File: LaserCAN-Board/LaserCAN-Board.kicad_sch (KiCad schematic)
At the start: 34 parts, among them J2 TC2050-IDC-NL, U10 M24C64-RMN6TP, U2 VL53L1CXV0FY1, U4 STM32F103C8Tx, U5 MCP1703Ax-330xxTT, U9 SN65HVD230

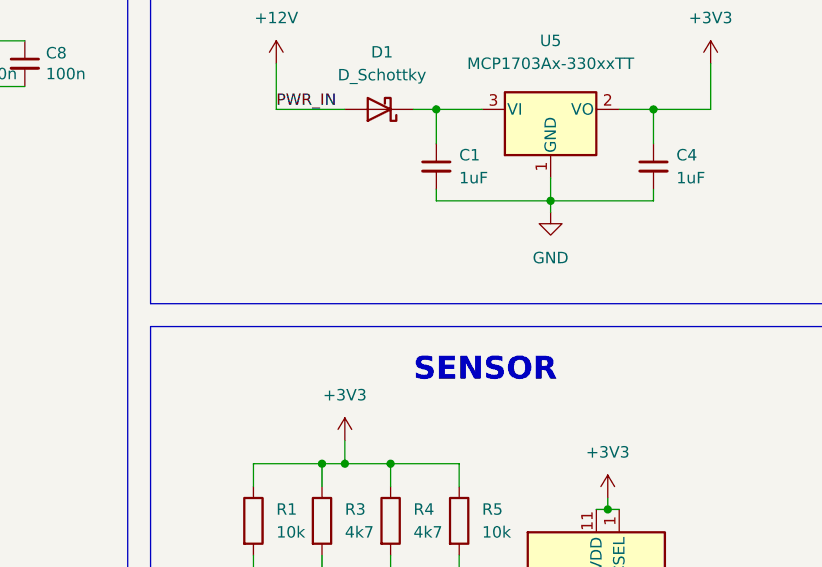
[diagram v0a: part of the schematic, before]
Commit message: Add PDF Schematic
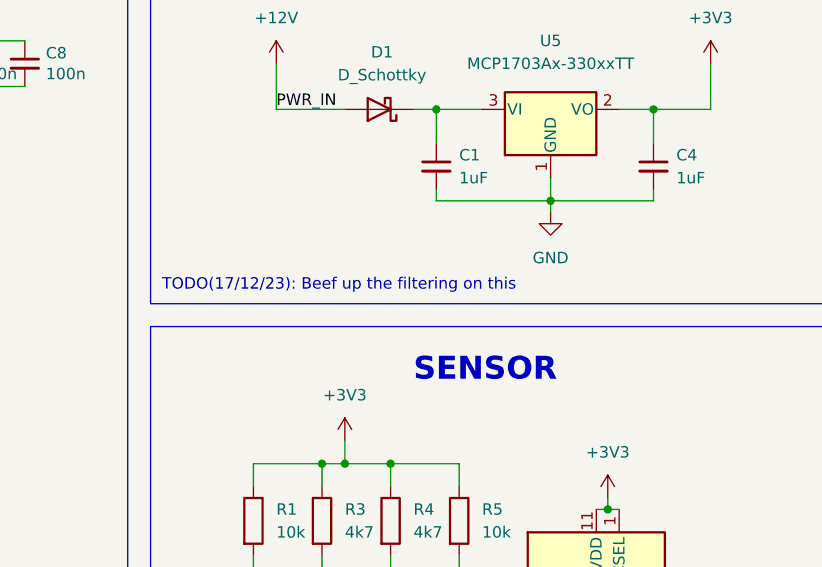
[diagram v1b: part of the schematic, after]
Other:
- note added: "TODO(17/12/23): Beef up the filtering on this"
- company: (none) -> Grapple Robotics
- title: (none) -> LaserCAN
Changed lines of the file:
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@@
 (kicad_sch (version 20230121) (generator eeschema)
   (paper "A4")
+  (title_block
+    (title "LaserCAN")
+    (rev "3")
+    (company "Grapple Robotics")
+    (comment 1 "https://grapplerobotics.au")
+    (comment 2 "https://github.com/GrappleRobotics/LaserCAN")
+  )
   (junction (at 203.2 111.76) (diameter 0) (color 0 0 0 0)
   )
@@
     (effects (font (size 2.54 2.54) (thickness 0.508) bold) (justify left bottom))
   )
+  (text "TODO(17/12/23): Beef up the filtering on this" (at 153.67 57.15 0)
+    (effects (font (size 1.27 1.27)) (justify left bottom))
+  )
   (label "CAN_RX" (at 106.68 69.85 180) (fields_autoplaced)

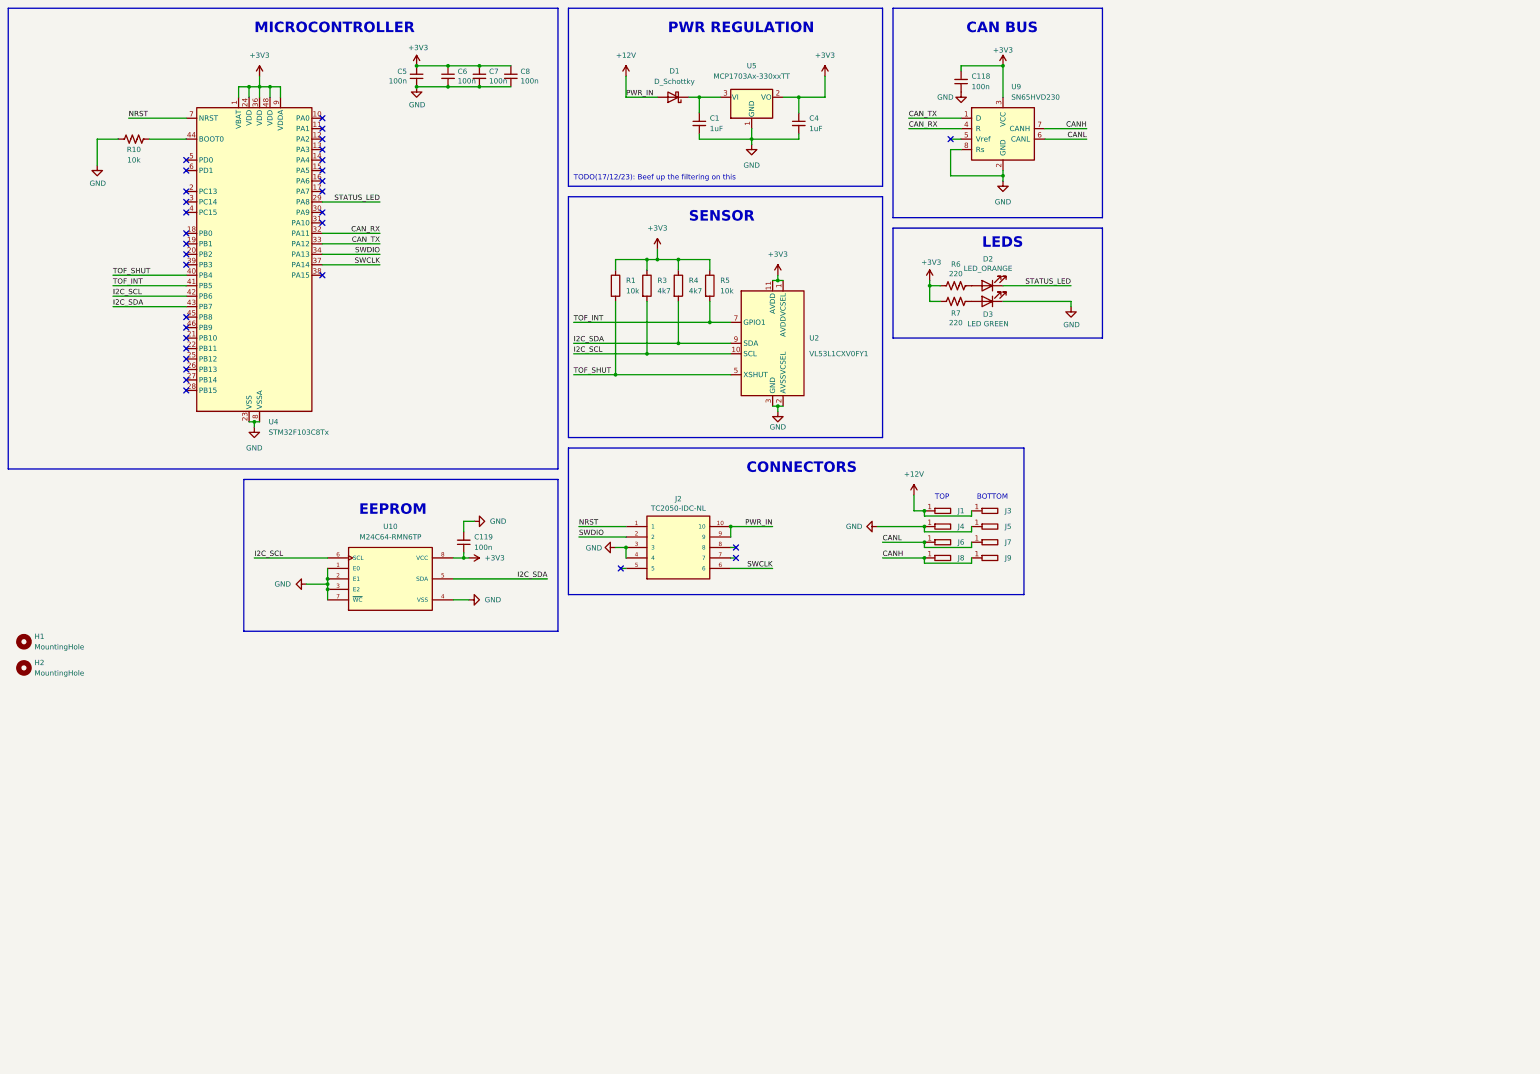
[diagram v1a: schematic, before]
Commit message: Update to v3.1 - Improved voltage regulation performance, improved ESD protection
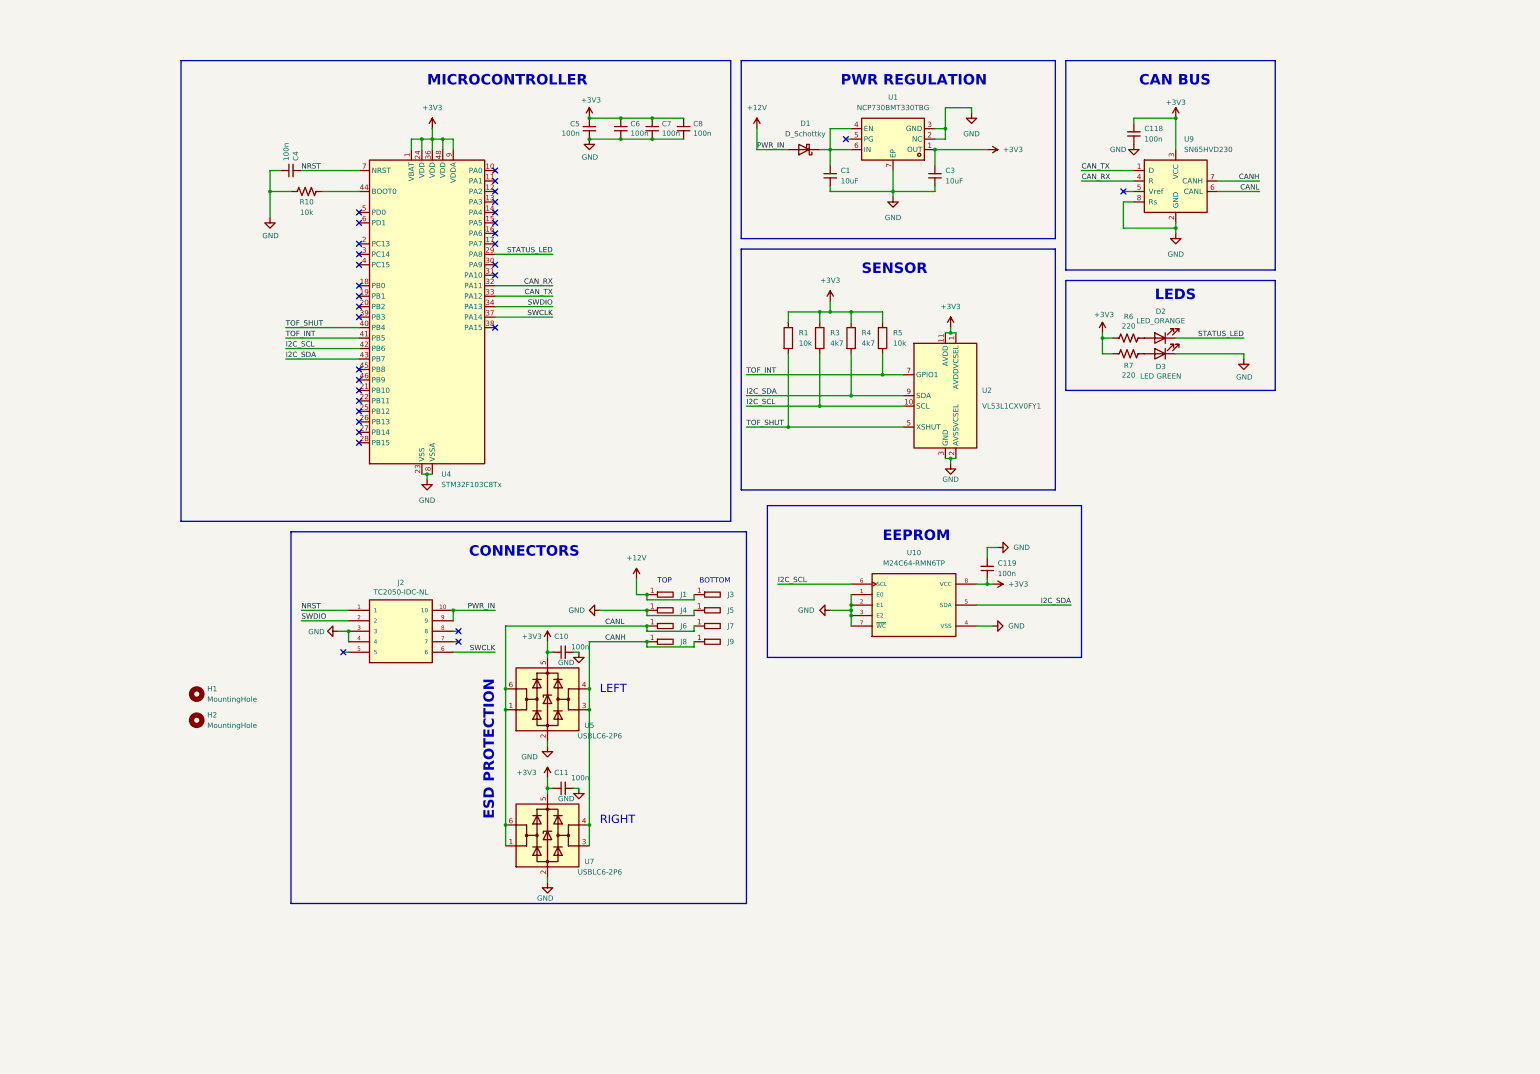
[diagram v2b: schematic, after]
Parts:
- removed U5: MCP1703Ax-330xxTT, Package_TO_SOT_SMD:SOT-23, symbol Regulator_Linear:MCP1703Ax-330xxTT
- added C10, C11: 100n, Capacitor_SMD:C_0402_1005Metric, symbol Device:C_Small
- added C3: 10uF, Capacitor_SMD:C_0603_1608Metric, symbol Device:C_Small
- added U1: NCP730BMT330TBG, NCP730BMT330TBG:WDFN-6_L2.0-W2.0-P0.65-BL-EP-1, symbol NCP730BMT330TBG:NCP730BMT330TBG
- added U5, U7: USBLC6-2P6, Package_TO_SOT_SMD:SOT-666, symbol Power_Protection:USBLC6-2P6
- C1: value 1uF -> 10uF; footprint Capacitor_SMD:C_0402_1005Metric -> Capacitor_SMD:C_0603_1608Metric; LCSC Part C52923 -> C96446
- C4: value 1uF -> 100n; LCSC Part C52923 -> C1525
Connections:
- net +3V3: now also C10.1, C11.1, C3.1, U1.1 (OUT), U5.5 (VBUS), U7.5 (VBUS); no longer C4.1
- net CANH: now also U5.3 (I/O2), U5.4 (I/O2), U7.3 (I/O2), U7.4 (I/O2)
- net CANL: now also U5.1 (I/O1), U5.6 (I/O1), U7.1 (I/O1), U7.6 (I/O1)
- net GND: now also C4.1, C10.2, C11.2, C3.2, U1.2 (NC), U1.3 (GND), U1.7 (EP), U5.2 (GND), U7.2 (GND); no longer C4.2
- net NRST: now also C4.2
- net at C1.1, D1.1 (K): now also U1.4 (EN), U1.6 (IN)
- no-connect marks 32 -> 33
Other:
- note added: "ESD PROTECTION"
- note added: "LEFT"
- note added: "RIGHT"
- note removed: "TODO(17/12/23): Beef up the filtering on this"
- moved on the sheet: C118, C119, C5, C6, C7, C8, D1, D2, D3, H1, H2, J1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

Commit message: Update to new power regulation circuitry
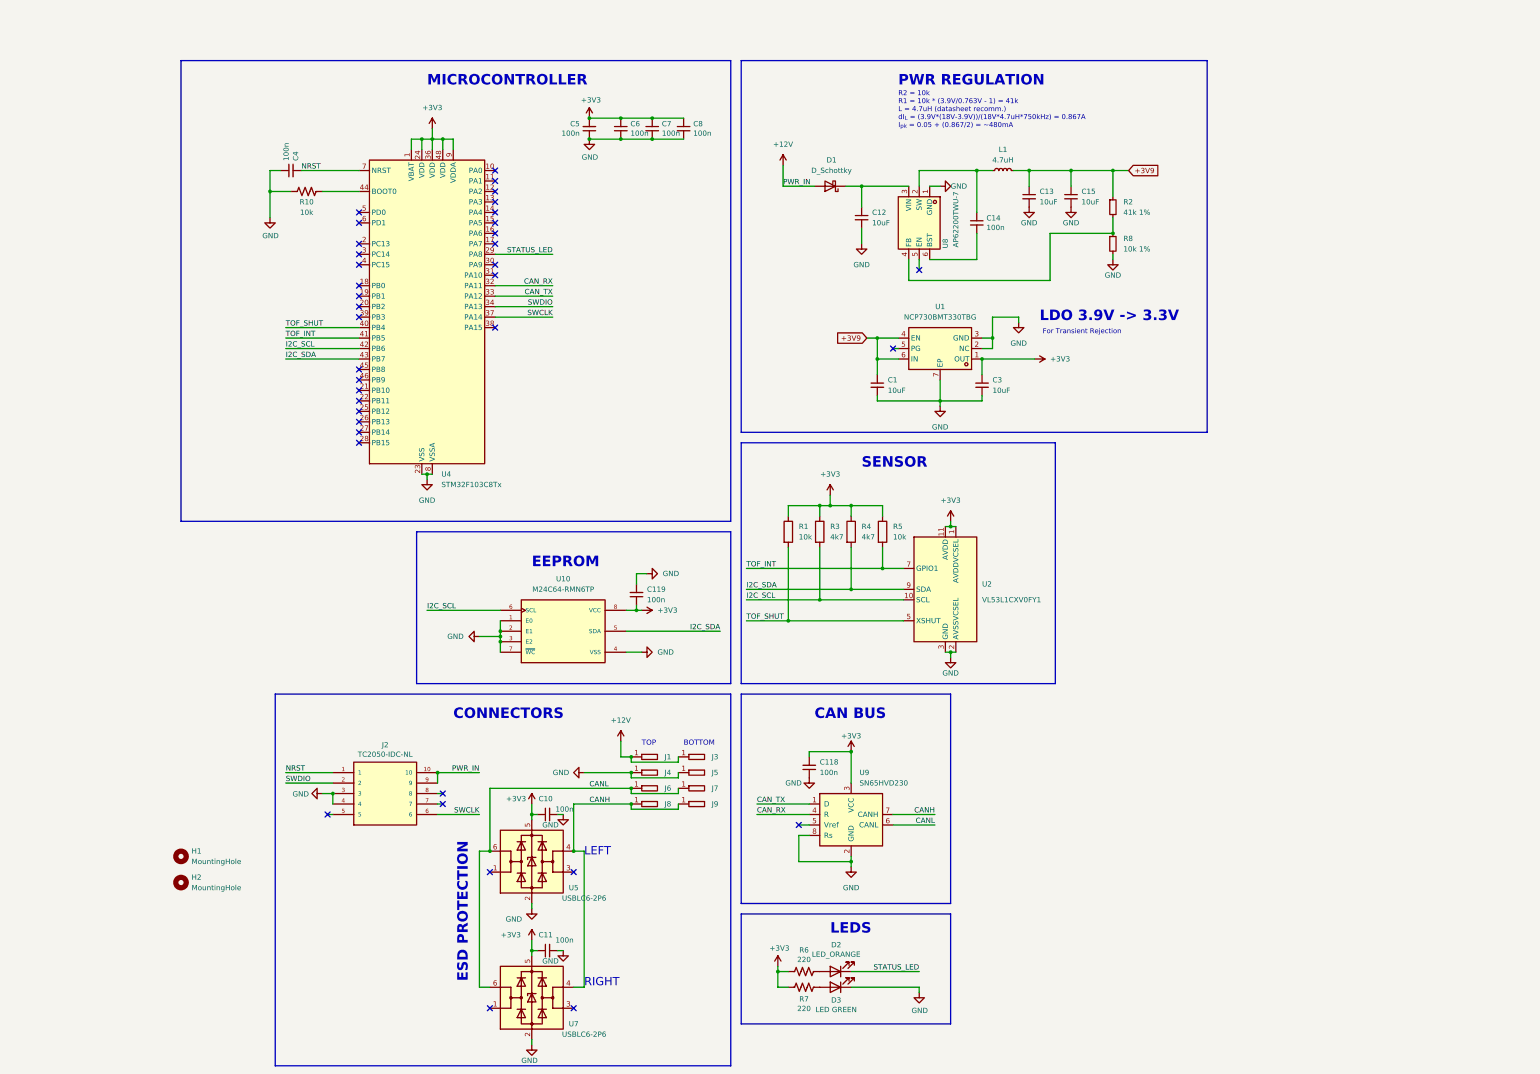
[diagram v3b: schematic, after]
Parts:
- added C12, C13, C15: 10uF, Capacitor_SMD:C_0603_1608Metric, symbol Device:C_Small
- added C14: 100n, Capacitor_SMD:C_0402_1005Metric, symbol Device:C_Small
- added L1: 4.7uH, Inductor_SMD:L_0805_2012Metric, symbol Device:L_Small
- added R2: 41k 1%, Resistor_SMD:R_0402_1005Metric, symbol Device:R_Small
- added R8: 10k 1%, Resistor_SMD:R_0402_1005Metric, symbol Device:R_Small
- added U8: AP62200TWU-7, AP62200TWU-7:TSOT-26_L2.9-W1.6-P0.95-LS2.8-BL, symbol AP62200TWU-7:AP62200TWU-7
- U5, U7: LCSC Part (none) -> C2827693
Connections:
- net CANH: no longer U5.3 (I/O2), U7.3 (I/O2)
- net CANL: no longer U5.1 (I/O1), U7.1 (I/O1)
- net GND: now also C12.2, C13.2, C15.2, R8.2, U8.1 (GND)
- net +3V9: now reaches C1.1, U1.4 (EN), U1.6 (IN)
- net +3V9: now also C13.1, C15.1, L1.2, R2.1; no longer D1.1 (K)
- new net: C12.1, D1.1 (K), U8.3 (VIN)
- new net: R2.2, R8.1, U8.4 (FB)
- new net: C14.1, L1.1, U8.2 (SW)
- new net: C14.2, U8.6 (BST)
- no-connect marks 33 -> 38
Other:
- note added: "For Transient Rejection"
- note added: "LDO 3.9V -> 3.3V"
- note added: "R2 = 10k R1 = 10k * (3.9V/0.763V - 1) = 41k L = 4.7uH (datasheet recomm.) dI_{L} = (3.9V*(18V-3.9V))/(18V*4.7uH*750kHz) = 0.867A I_{pk} = 0.05 + (0.867/2) = ~480mA"
- moved on the sheet: C1, C10, C11, C118, C119, C3, D2, D3, H1, H2, J1, J2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

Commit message: Add new power regulation, completely re-route board to accomodate
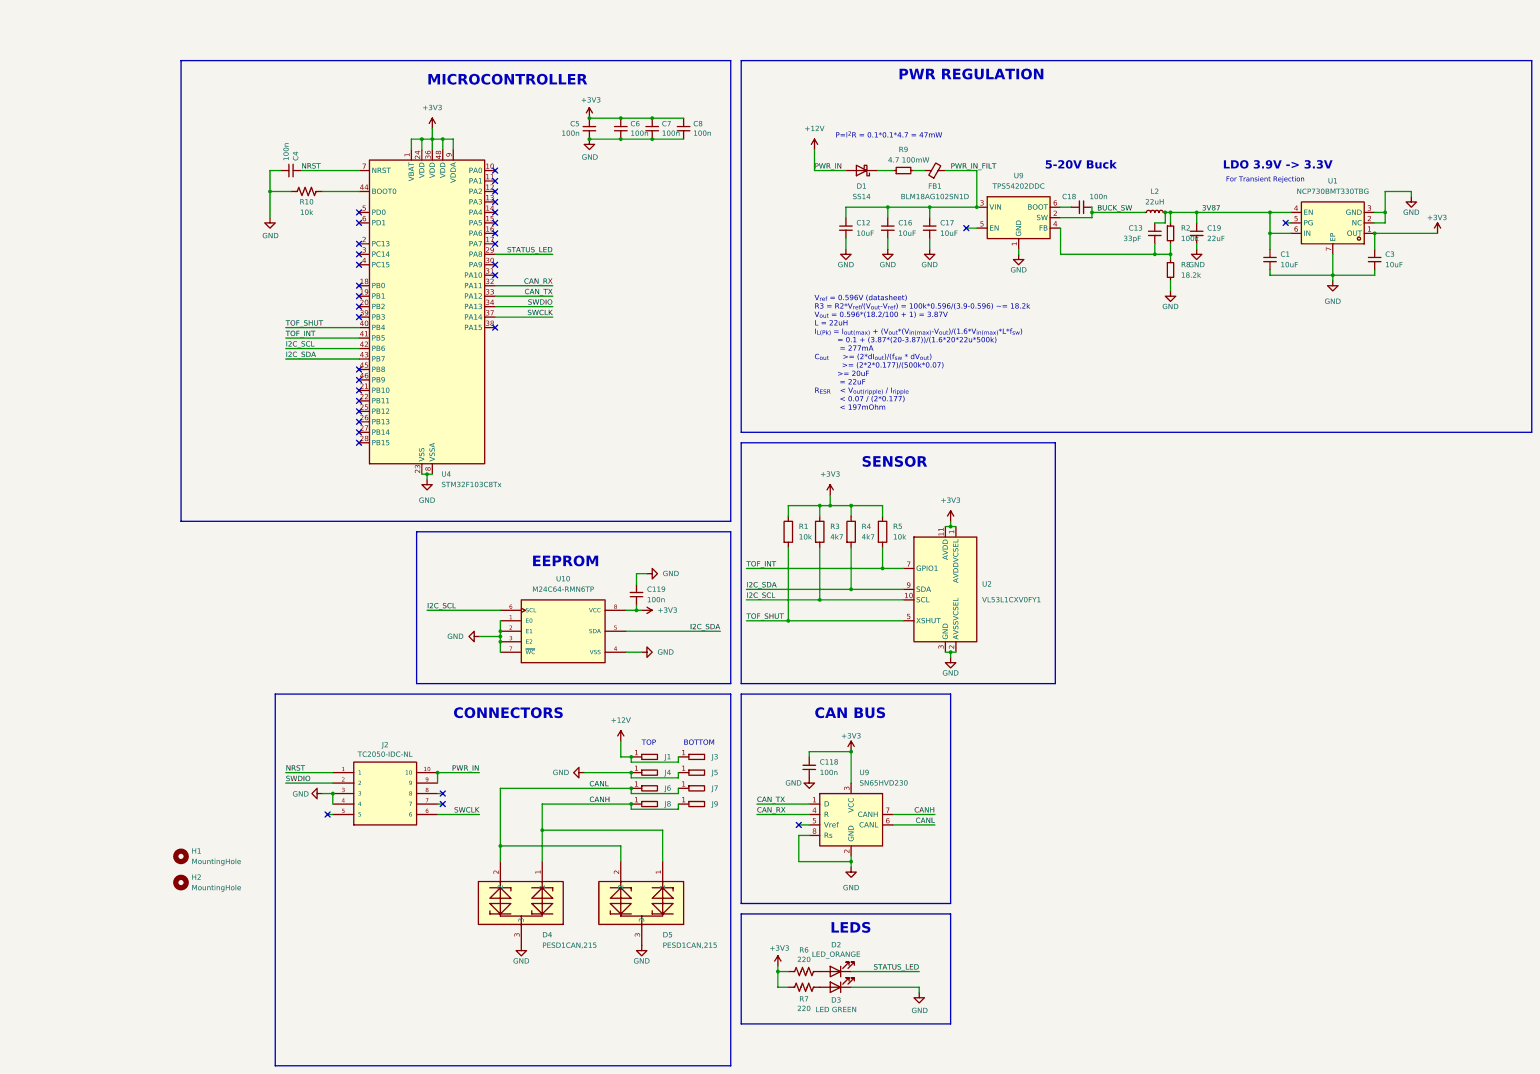
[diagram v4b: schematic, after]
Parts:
- removed C10, C11, C14: 100n, Capacitor_SMD:C_0402_1005Metric, symbol Device:C_Small
- removed C15: 10uF, Capacitor_SMD:C_0603_1608Metric, symbol Device:C_Small
- removed L1: 4.7uH, Inductor_SMD:L_0805_2012Metric, symbol Device:L_Small
- removed U5, U7: USBLC6-2P6, Package_TO_SOT_SMD:SOT-666, symbol Power_Protection:USBLC6-2P6
- removed U8: AP62200TWU-7, AP62200TWU-7:TSOT-26_L2.9-W1.6-P0.95-LS2.8-BL, symbol AP62200TWU-7:AP62200TWU-7
- added C16, C17: 10uF, Capacitor_SMD:C_0603_1608Metric, symbol Device:C_Small
- added C18: 100n, Capacitor_SMD:C_0402_1005Metric, symbol Device:C_Small
- added C19: 22uF, Capacitor_SMD:C_0805_2012Metric, symbol Device:C_Small
- added D4, D5: PESD1CAN,215, PESD1CAN:SOT-23_L2.9-W1.3-P1.90-LS2.4-BR, symbol PESD1CAN:PESD1CAN,215
- added FB1: BLM18AG102SN1D, Inductor_SMD:L_0603_1608Metric, symbol Device:FerriteBead_Small
- added L2: 22uH, Inductor_SMD:L_1008_2520Metric, symbol Device:L_Small
- added R9: 4.7 100mW, Resistor_SMD:R_0603_1608Metric, symbol Device:R_Small
- added U9: TPS54202DDC, Package_TO_SOT_SMD:SOT-23-6, symbol Regulator_Switching:TPS54202DDC
- C13: value 10uF -> 33pF; footprint Capacitor_SMD:C_0603_1608Metric -> Capacitor_SMD:C_0402_1005Metric; LCSC Part C96446 -> C1562
- D1: value D_Schottky -> SS14
- R2: value 41k 1% -> 100k; LCSC Part C185416 -> C25741
- R8: value 10k 1% -> 18.2k; LCSC Part C25744 -> C226826
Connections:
- net CANH: now also D4.1, D5.1
- net CANL: now also D4.2, D5.2
- net GND: now also C16.2, C17.2, C19.2, D4.3, D5.3, U9.1 (GND); no longer C13.2
- net at D1.1 (K): now also R9.1; no longer C12.1
- net at R2.2, R8.1: now also C13.2, U9.4 (FB)
- net +3V9 renamed 3V87
- net 3V87: now also C19.1, L2.2
- new net: C18.1, U9.6 (BOOT)
- new net: FB1.1, R9.2
- new net BUCK_SW: C18.2, L2.1, U9.2 (SW)
- new net PWR_IN_FILT: C12.1, C16.1, C17.1, FB1.2, U9.3 (VIN)
- no-connect marks 38 -> 34
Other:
- note added: "5-20V Buck"
- note added: "P=I^{2}R = 0.1*0.1*4.7 = 47mW"
- note added: "V_{ref} = 0.596V (datasheet) R3 = R2*V_{ref}/(V_{out}-V_{ref}) = 100k*0.596/(3.9-0.596) ~= 18.2k V_{out} = 0.596*(18.2/100 + 1) = 3.87V L = 22uH I_{L(Pk)} = I_{out(max)} + (V_{out}*(V_{in(max)}-V_{out})/(1.6*V_{in(max)}*L*f_{sw}) = 0.1 + (3.87*(20-3.87))/(1.6*20*22u*500k) = 277mA C_{out} >= (2*dI_{out})/(f_{sw} * dV_{out}) >= (2*2*0.177)/(500k*0.07) >= 20uF = 22uF R_{ESR} < V_{out(ripple)} / I_{r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"
- note removed: "ESD PROTECTION"
- note removed: "LEFT"
- note removed: "R2 = 10k R1 = 10k * (3.9V/0.763V - 1) = 41k L = 4.7uH (datasheet recomm.) dI_{L} = (3.9V*(18V-3.9V))/(18V*4.7uH*750kHz) = 0.867A I_{pk} = 0.05 + (0.867/2) = ~480mA"
- note removed: "RIGHT"
- moved on the sheet: C1, C3, U1
